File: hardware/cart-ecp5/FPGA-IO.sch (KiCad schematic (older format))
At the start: 9 parts, among them J1 JTAG, U1 LFE5U-25F-xBG256x, U2 W25Q512JVEIM, X1 XO_Generic_NC

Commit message: Substitute QE=1 config flash to keep boot time as short as possible
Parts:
- removed U2: W25Q512JVEIM, Package_SON:WSON-8-1EP_6x5mm_P1.27mm_EP3.4x4.3mm, symbol ng_memory:W25Q512JVEIM
- added U2: W25Q128JVPIQ, Package_SON:WSON-8-1EP_6x5mm_P1.27mm_EP3.4x4mm, symbol ng_memory:W25Q128JVPIQ
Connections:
- net labels added: FPGA_CDONE
- wire segments 55 -> 56
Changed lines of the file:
@@
 Wire Wire Line
 	10200 4300 10300 4300
-$Comp
-L ng_power:GND #PWR03
-U 1 1 5F643215
-P 10400 1600
-F 0 "#PWR03" H 10400 1350 50  0001 C CNN
-F 1 "GND" V 10404 1520 50  0000 R CNN
-F 2 "" H 10300 1250 50  0001 C CNN
-F 3 "" H 10400 1600 50  0001 C CNN
-	1    10400 1600
-	0    -1   -1   0
-$EndComp
 Wire Wire Line
 	10200 1600 10300 1600
@@
 Wire Wire Line
 	10300 1800 10300 1600
-Connection ~ 10300 1600
-Wire Wire Line
-	10300 1600 10400 1600
 Wire Wire Line
 	10200 1700 10500 1700
@@
 Text GLabel 10200 6700 2    50   Input ~ 0
 SD_CD
-$Comp
-L ng_memory:W25Q512JVEIM U2
-U 1 1 5F5A1820
-P 13200 1500
-F 0 "U2" H 13650 1665 50  0000 C CNN
-F 1 "W25Q512JVEIM" H 13650 1574 50  0000 C CNN
-F 2 "Package_SON:WSON-8-1EP_6x5mm_P1.27mm_EP3.4x4.3mm" H 13650 650 50  0001 C CNN
-F 3 "https://www.winbond.com/resource-files/W25Q512JV%20DTR%20RevC%2009102019%20133.pdf" H 14200 1200 50  0001 C CNN
-	1    13200 1500
-	-1   0    0    -1
-$EndComp
 Text GLabel 6700 5700 2    50   BiDi ~ 0
 USB_AD0
@@
 Text Label 3300 8400 0    50   ~ 0
 REF_CLK
+$Comp
+L ng_memory:W25Q128JVPIQ U2
+U 1 1 5FC54331
+P 13200 1500
+F 0 "U2" H 13650 1665 50  0000 C CNN
+F 1 "W25Q128JVPIQ" H 13650 1574 50  0000 C CNN
+F 2 "Package_SON:WSON-8-1EP_6x5mm_P1.27mm_EP3.4x4mm" H 13700 650 50  0001 C CNN
+F 3 "https://www.mouser.com/datasheet/2/949/w25q128jv_revf_03272018_plus-1489608.pdf" H 14200 1200 50  0001 C CNN
+	1    13200 1500
+	-1   0    0    -1
+$EndComp
+Wire Wire Line
+	10200 2100 11050 2100
+Text GLabel 11050 2100 2    50   Output ~ 0
+FPGA_CDONE
+Connection ~ 10300 1600
+Wire Wire Line
+	10300 1600 10400 1600
+$Comp
+L ng_power:GND #PWR03
+U 1 1 5F643215
+P 10400 1600
+F 0 "#PWR03" H 10400 1350 50  0001 C CNN
+F 1 "GND" V 10404 1520 50  0000 R CNN
+F 2 "" H 10300 1250 50  0001 C CNN
+F 3 "" H 10400 1600 50  0001 C CNN
+	1    10400 1600
+	0    -1   -1   0
+$EndComp
 $EndSCHEMATC

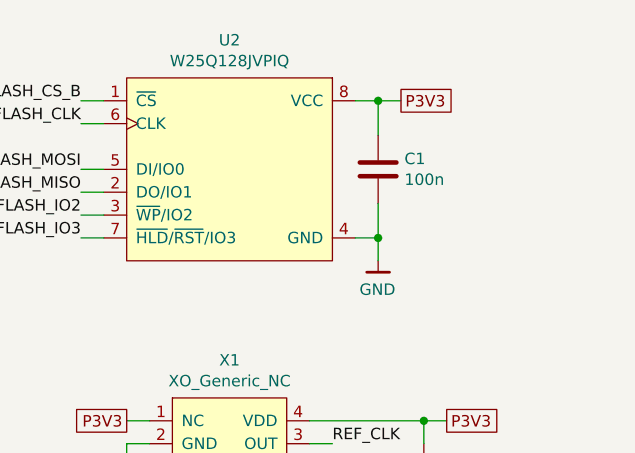
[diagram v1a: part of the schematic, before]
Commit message: Fix the configuration flash's decoupling capacitor
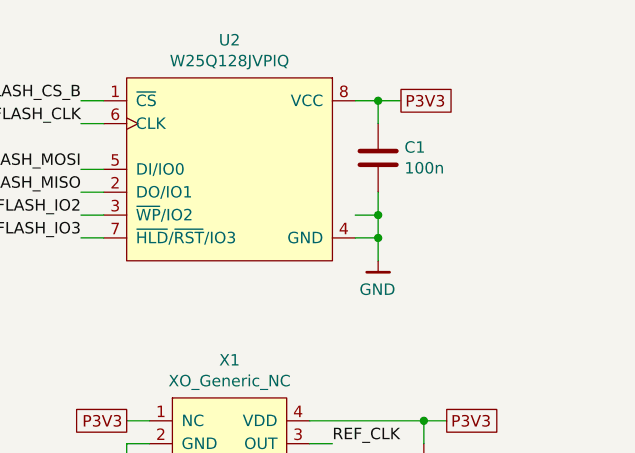
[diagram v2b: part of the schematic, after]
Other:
- moved on the sheet: C1
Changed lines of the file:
@@
 L Device:C C1
 U 1 1 5F81782E
-P 13400 1900
-F 0 "C1" H 13515 1946 50  0000 L CNN
-F 1 "100n" H 13515 1855 50  0000 L CNN
-F 2 "Capacitor_SMD:C_0402_1005Metric" H 13438 1750 50  0001 C CNN
-F 3 "~" H 13400 1900 50  0001 C CNN
-	1    13400 1900
+P 13400 1850
+F 0 "C1" H 13515 1896 50  0000 L CNN
+F 1 "100n" H 13515 1805 50  0000 L CNN
+F 2 "Capacitor_SMD:C_0402_1005Metric" H 13438 1700 50  0001 C CNN
+F 3 "~" H 13400 1850 50  0001 C CNN
+	1    13400 1850
 	1    0    0    -1
 $EndComp
 Wire Wire Line
-	13400 1750 13400 1600
+	13400 1700 13400 1600
 Wire Wire Line
 	13400 1600 13300 1600
@@
 	13300 2200 13400 2200
 Wire Wire Line
-	13400 2200 13400 2050
+	13400 2200 13400 2100
 Wire Wire Line
 	13400 1600 13500 1600
@@
 	0    -1   -1   0
 $EndComp
+Wire Wire Line
+	13300 2100 13400 2100
+Connection ~ 13400 2100
+Wire Wire Line
+	13400 2100 13400 2000
 $EndSCHEMATC

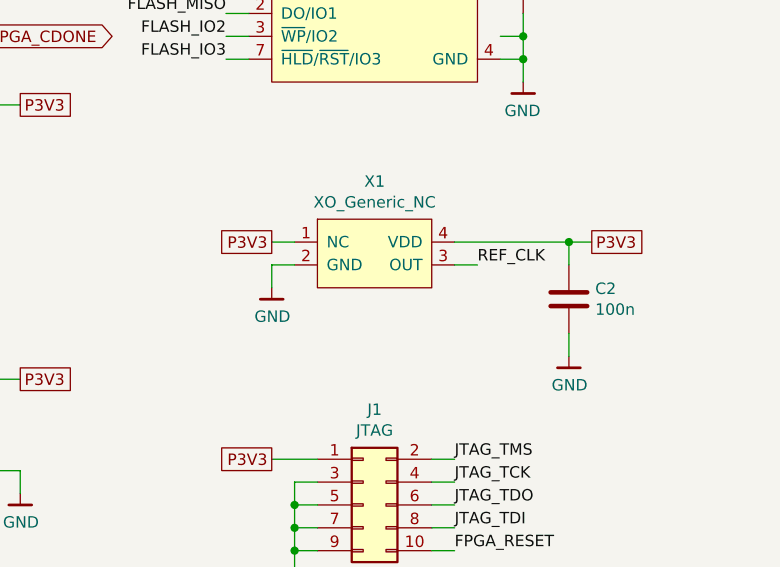
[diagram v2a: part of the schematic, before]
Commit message: Add testpoints for clock oscillator outputs
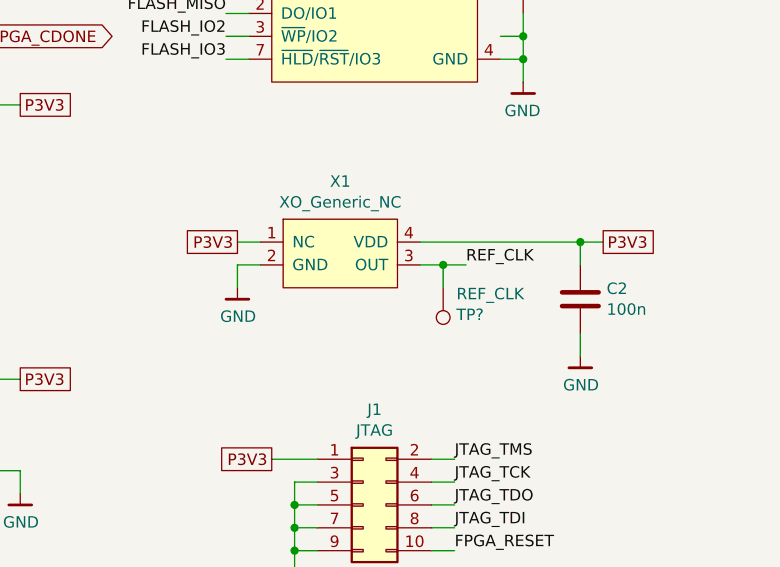
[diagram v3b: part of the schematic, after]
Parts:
- added TP?: REF_CLK, symbol Connector:TestPoint
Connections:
- net REF_CLK: now also TP?.1
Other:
- moved on the sheet: C2, X1
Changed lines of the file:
@@
 L ng_time:XO_Generic_NC X1
 U 1 1 5F7FED75
-P 12750 3050
-F 0 "X1" H 12750 3365 50  0000 C CNN
-F 1 "XO_Generic_NC" H 12750 3274 50  0000 C CNN
-F 2 "ng_time:Oscillator_2.5x2.0" H 12750 2950 50  0001 C CNN
-F 3 "" H 12750 2950 50  0001 C CNN
-	1    12750 3050
-	1    0    0    -1
-$EndComp
-Wire Wire Line
-	12400 3100 12300 3100
-Wire Wire Line
-	12300 3100 12300 3200
-Wire Wire Line
-	12400 3000 12300 3000
-Text GLabel 13700 3000 2    50   UnSpc ~ 0
+P 12600 3050
+F 0 "X1" H 12600 3365 50  0000 C CNN
+F 1 "XO_Generic_NC" H 12600 3274 50  0000 C CNN
+F 2 "ng_time:Oscillator_2.5x2.0" H 12600 2950 50  0001 C CNN
+F 3 "" H 12600 2950 50  0001 C CNN
+	1    12600 3050
+	1    0    0    -1
+$EndComp
+Wire Wire Line
+	12250 3100 12150 3100
+Wire Wire Line
+	12150 3100 12150 3200
+Wire Wire Line
+	12250 3000 12150 3000
+Text GLabel 13750 3000 2    50   UnSpc ~ 0
 P3V3
-Text GLabel 12300 3000 0    50   UnSpc ~ 0
+Text GLabel 12150 3000 0    50   UnSpc ~ 0
 P3V3
 $Comp
 L ng_power:GND #PWR05
 U 1 1 5F809997
-P 12300 3200
-F 0 "#PWR05" H 12300 2950 50  0001 C CNN
-F 1 "GND" H 12303 3074 50  0000 C CNN
-F 2 "" H 12200 2850 50  0001 C CNN
-F 3 "" H 12300 3200 50  0001 C CNN
-	1    12300 3200
+P 12150 3200
+F 0 "#PWR05" H 12150 2950 50  0001 C CNN
+F 1 "GND" H 12153 3074 50  0000 C CNN
+F 2 "" H 12050 2850 50  0001 C CNN
+F 3 "" H 12150 3200 50  0001 C CNN
+	1    12150 3200
 	1    0    0    -1
 $EndComp
@@
 L Device:C C2
 U 1 1 5F839810
-P 13600 3250
-F 0 "C2" H 13715 3296 50  0000 L CNN
-F 1 "100n" H 13715 3205 50  0000 L CNN
-F 2 "Capacitor_SMD:C_0402_1005Metric" H 13638 3100 50  0001 C CNN
-F 3 "~" H 13600 3250 50  0001 C CNN
-	1    13600 3250
-	1    0    0    -1
-$EndComp
-Wire Wire Line
-	13600 3100 13600 3000
-Wire Wire Line
-	13600 3000 13700 3000
+P 13650 3250
+F 0 "C2" H 13765 3296 50  0000 L CNN
+F 1 "100n" H 13765 3205 50  0000 L CNN
+F 2 "Capacitor_SMD:C_0402_1005Metric" H 13688 3100 50  0001 C CNN
+F 3 "~" H 13650 3250 50  0001 C CNN
+	1    13650 3250
+	1    0    0    -1
+$EndComp
+Wire Wire Line
+	13650 3100 13650 3000
+Wire Wire Line
+	13650 3000 13750 3000
 $Comp
 L ng_power:GND #PWR08
 U 1 1 5F83DBF8
-P 13600 3500
-F 0 "#PWR08" H 13600 3250 50  0001 C CNN
-F 1 "GND" H 13603 3374 50  0000 C CNN
-F 2 "" H 13500 3150 50  0001 C CNN
-F 3 "" H 13600 3500 50  0001 C CNN
-	1    13600 3500
-	1    0    0    -1
-$EndComp
-Wire Wire Line
-	13600 3400 13600 3500
-Wire Wire Line
-	13600 3000 13100 3000
-Connection ~ 13600 3000
-Wire Wire Line
-	13100 3100 13200 3100
-Text Label 13200 3100 0    50   ~ 0
+P 13650 3500
+F 0 "#PWR08" H 13650 3250 50  0001 C CNN
+F 1 "GND" H 13653 3374 50  0000 C CNN
+F 2 "" H 13550 3150 50  0001 C CNN
+F 3 "" H 13650 3500 50  0001 C CNN
+	1    13650 3500
+	1    0    0    -1
+$EndComp
+Wire Wire Line
+	13650 3400 13650 3500
+Wire Wire Line
+	13650 3000 12950 3000
+Connection ~ 13650 3000
+Wire Wire Line
+	12950 3100 13050 3100
+Text Label 13150 3100 0    50   ~ 0
 REF_CLK
 Text GLabel 3200 1600 2    50   Input ~ 0
@@
 Wire Wire Line
 	13400 2100 13400 2000
+Wire Wire Line
+	13050 3100 13050 3200
+$Comp
+L Connector:TestPoint TP?
+U 1 1 5FDC5F08
+P 13050 3200
+AR Path="/5F483803/5FDC5F08" Ref="TP?"  Part="1"
+AR Path="/5F3E46DE/5FDC5F08" Ref="TP?"  Part="1"
+F 0 "TP?" H 13108 3318 50  0000 L CNN
+F 1 "REF_CLK" H 13108 3227 50  0000 L CNN
+F 2 "" H 13250 3200 50  0001 C CNN
+F 3 "~" H 13250 3200 50  0001 C CNN
+	1    13050 3200
+	1    0    0    1
+$EndComp
+Connection ~ 13050 3100
+Wire Wire Line
+	13050 3100 13150 3100
 $EndSCHEMATC

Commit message: Layout testpoints for power rails and clock oscillators
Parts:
- TP1: renamed from TP?; footprint (none) -> ng_test:TestPoint_Pad_D0.5mm
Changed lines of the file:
@@
 P 13050 3200
 AR Path="/5F483803/5FDC5F08" Ref="TP?"  Part="1"
-AR Path="/5F3E46DE/5FDC5F08" Ref="TP?"  Part="1"
-F 0 "TP?" H 13108 3318 50  0000 L CNN
+AR Path="/5F3E46DE/5FDC5F08" Ref="TP1"  Part="1"
+F 0 "TP1" H 13108 3318 50  0000 L CNN
 F 1 "REF_CLK" H 13108 3227 50  0000 L CNN
-F 2 "" H 13250 3200 50  0001 C CNN
+F 2 "ng_test:TestPoint_Pad_D0.5mm" H 13250 3200 50  0001 C CNN
 F 3 "~" H 13250 3200 50  0001 C CNN
 	1    13050 3200

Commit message: Don't stuff the net name into test point values
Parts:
- TP1: value REF_CLK -> TestPoint
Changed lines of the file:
@@
 AR Path="/5F3E46DE/5FDC5F08" Ref="TP1"  Part="1"
 F 0 "TP1" H 13108 3318 50  0000 L CNN
-F 1 "REF_CLK" H 13108 3227 50  0000 L CNN
+F 1 "TestPoint" H 13108 3227 50  0001 L CNN
 F 2 "ng_test:TestPoint_Pad_D0.5mm" H 13250 3200 50  0001 C CNN
 F 3 "~" H 13250 3200 50  0001 C CNN

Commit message: Enlarge test points to 1mm diameter
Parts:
- TP1: footprint ng_test:TestPoint_Pad_D0.5mm -> TestPoint:TestPoint_Pad_D1.0mm
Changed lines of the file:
@@
 F 0 "TP1" H 13108 3318 50  0000 L CNN
 F 1 "TestPoint" H 13108 3227 50  0001 L CNN
-F 2 "ng_test:TestPoint_Pad_D0.5mm" H 13250 3200 50  0001 C CNN
+F 2 "TestPoint:TestPoint_Pad_D1.0mm" H 13250 3200 50  0001 C CNN
 F 3 "~" H 13250 3200 50  0001 C CNN
 	1    13050 3200

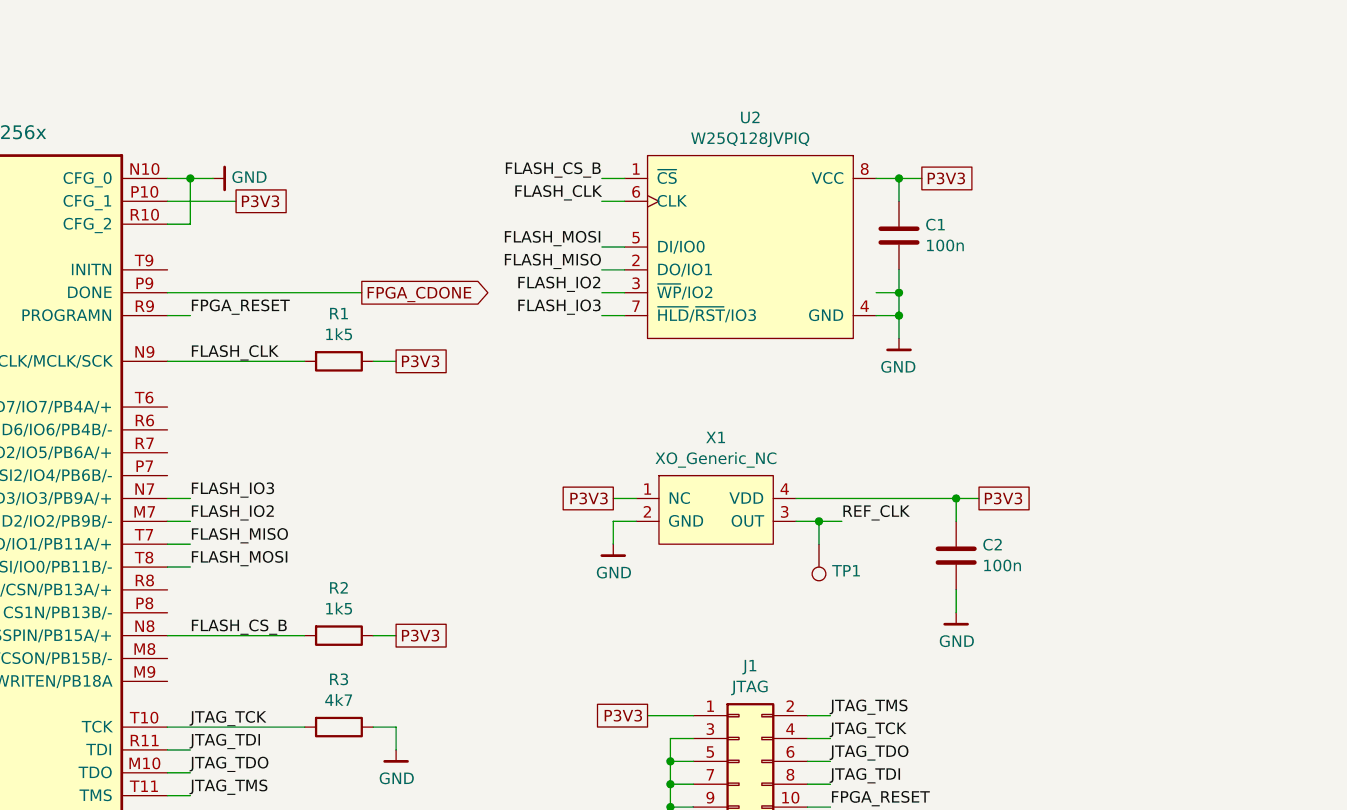
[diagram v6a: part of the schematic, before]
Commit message: Clarify pull-up design for configuration flash and FPGA reset signal
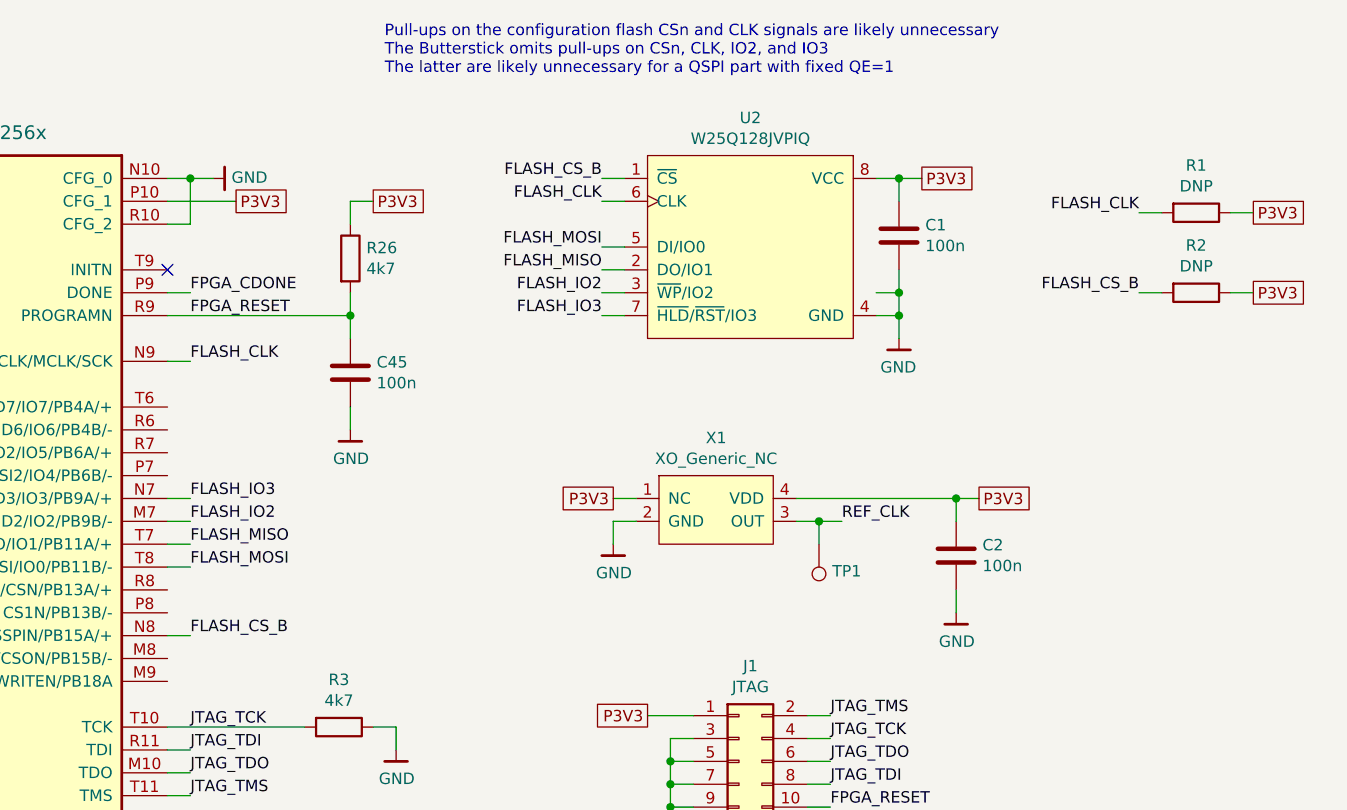
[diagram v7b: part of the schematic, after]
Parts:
- added C45: 100n, Capacitor_SMD:C_0402_1005Metric, symbol Device:C
- added R26: 4k7, Resistor_SMD:R_0402_1005Metric, symbol Device:R
- R1, R2: value 1k5 -> DNP
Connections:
- net FPGA_RESET: now also C45.1, R26.2
- net GND: now also C45.2
- net P3V3: now also R26.1
- no-connect marks 0 -> 1
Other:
- note added: "Pull-ups on the configuration flash CSn and CLK signals are likely unnecessary\nThe Butterstick omits pull-ups on CSn, CLK, IO2, and IO3\nThe latter are likely unnecessary for a QSPI part with fixed QE=1"
- moved on the sheet: R1, R2
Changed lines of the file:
@@
 $EndComp
 Wire Wire Line
-	10200 3600 10800 3600
-Wire Wire Line
-	10200 2400 10800 2400
+	10200 3600 10300 3600
+Wire Wire Line
+	10200 2400 10300 2400
 Wire Wire Line
 	10200 3300 10300 3300
@@
 P3V3
 Wire Wire Line
-	10200 2200 10300 2200
+	10200 2200 11000 2200
 $Comp
 L Device:R R3
@@
 Text Label 10300 2200 0    50   ~ 0
 FPGA_RESET
-$Comp
-L Device:R R1
-U 1 1 5F67946D
-P 10950 2400
-F 0 "R1" V 10743 2400 50  0000 C CNN
-F 1 "1k5" V 10834 2400 50  0000 C CNN
-F 2 "Resistor_SMD:R_0402_1005Metric" V 10880 2400 50  0001 C CNN
-F 3 "~" H 10950 2400 50  0001 C CNN
-	1    10950 2400
-	0    1    1    0
-$EndComp
-Wire Wire Line
-	11100 2400 11200 2400
+Wire Wire Line
+	14850 1750 14950 1750
 $Comp
 L Device:R R2
 U 1 1 5F67D9E4
-P 10950 3600
-F 0 "R2" V 10743 3600 50  0000 C CNN
-F 1 "1k5" V 10834 3600 50  0000 C CNN
-F 2 "Resistor_SMD:R_0402_1005Metric" V 10880 3600 50  0001 C CNN
-F 3 "~" H 10950 3600 50  0001 C CNN
-	1    10950 3600
+P 14700 2100
+F 0 "R2" V 14493 2100 50  0000 C CNN
+F 1 "DNP" V 14584 2100 50  0000 C CNN
+F 2 "Resistor_SMD:R_0402_1005Metric" V 14630 2100 50  0001 C CNN
+F 3 "~" H 14700 2100 50  0001 C CNN
+	1    14700 2100
 	0    1    1    0
 $EndComp
 Wire Wire Line
-	11100 3600 11200 3600
-Text GLabel 11200 3600 2    50   UnSpc ~ 0
-P3V3
-Text GLabel 11200 2400 2    50   UnSpc ~ 0
+	14850 2100 14950 2100
+Text GLabel 14950 2100 2    50   UnSpc ~ 0
+P3V3
+Text GLabel 14950 1750 2    50   UnSpc ~ 0
 P3V3
 $Comp
@@
 	-1   0    0    -1
 $EndComp
-Wire Wire Line
-	10200 2100 11050 2100
-Text GLabel 11050 2100 2    50   Output ~ 0
-FPGA_CDONE
 Connection ~ 10300 1600
 Wire Wire Line
@@
 Wire Wire Line
 	13050 3100 13150 3100
+$Comp
+L Device:R R1
+U 1 1 5F67946D
+P 14700 1750
+F 0 "R1" V 14493 1750 50  0000 C CNN
+F 1 "DNP" V 14584 1750 50  0000 C CNN
+F 2 "Resistor_SMD:R_0402_1005Metric" V 14630 1750 50  0001 C CNN
+F 3 "~" H 14700 1750 50  0001 C CNN
+	1    14700 1750
+	0    1    1    0
+$EndComp
+Wire Wire Line
+	11000 1700 11100 1700
+Text GLabel 11100 1700 2    50   UnSpc ~ 0
+P3V3
+Text Notes 11150 1150 0    50   ~ 0
+Pull-ups on the configuration flash CSn and CLK signals are likely unnecessary\nThe Butterstick omits pull-ups on CSn, CLK, IO2, and IO3\nThe latter are likely unnecessary for a QSPI part with fixed QE=1
+Wire Wire Line
+	14550 1750 14450 1750
+Wire Wire Line
+	14550 2100 14450 2100
+Text Label 14450 2100 2    50   ~ 0
+FLASH_CS_B
+Text Label 14450 1750 2    50   ~ 0
+FLASH_CLK
+$Comp
+L Device:R R26
+U 1 1 5FF8D4D1
+P 11000 1950
+F 0 "R26" H 11070 1996 50  0000 L CNN
+F 1 "4k7" H 11070 1905 50  0000 L CNN
+F 2 "Resistor_SMD:R_0402_1005Metric" V 10930 1950 50  0001 C CNN
+F 3 "~" H 11000 1950 50  0001 C CNN
+	1    11000 1950
+	1    0    0    -1
+$EndComp
+Wire Wire Line
+	10200 2100 10300 2100
+Text Label 10300 2100 0    50   ~ 0
+FPGA_CDONE
+NoConn ~ 10200 2000
+$Comp
+L Device:C C45
+U 1 1 5FF9EFF4
+P 11000 2450
+F 0 "C45" H 11115 2496 50  0000 L CNN
+F 1 "100n" H 11115 2405 50  0000 L CNN
+F 2 "Capacitor_SMD:C_0402_1005Metric" H 11038 2300 50  0001 C CNN
+F 3 "~" H 11000 2450 50  0001 C CNN
+	1    11000 2450
+	1    0    0    -1
+$EndComp
+Wire Wire Line
+	11000 2200 11000 2100
+Wire Wire Line
+	11000 2200 11000 2300
+Connection ~ 11000 2200
+Wire Wire Line
+	11000 2600 11000 2700
+$Comp
+L ng_power:GND #PWR072
+U 1 1 5FFA7EA6
+P 11000 2700
+F 0 "#PWR072" H 11000 2450 50  0001 C CNN
+F 1 "GND" H 11003 2574 50  0000 C CNN
+F 2 "" H 10900 2350 50  0001 C CNN
+F 3 "" H 11000 2700 50  0001 C CNN
+	1    11000 2700
+	1    0    0    -1
+$EndComp
+Wire Wire Line
+	11000 1700 11000 1800
 $EndSCHEMATC
